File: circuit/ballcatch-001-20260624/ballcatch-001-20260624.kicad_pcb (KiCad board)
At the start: 2 copper layers, 55.6 x 32.2 mm, 5 parts, among them J1 Conn_01x03_Pin, Q1 Q_Photo_NPN_CE

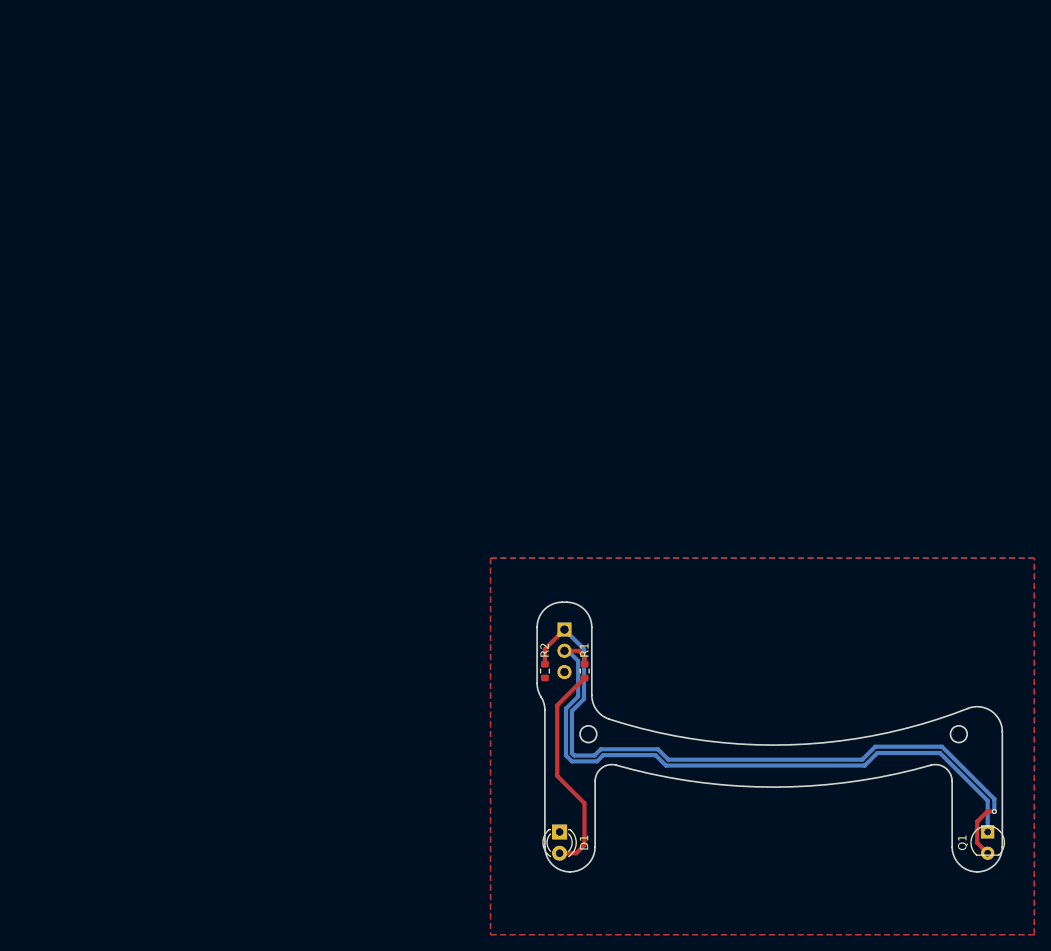
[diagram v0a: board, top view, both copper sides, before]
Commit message: Update ボール補足センサのDR完了、JLCPCBのロゴ追加
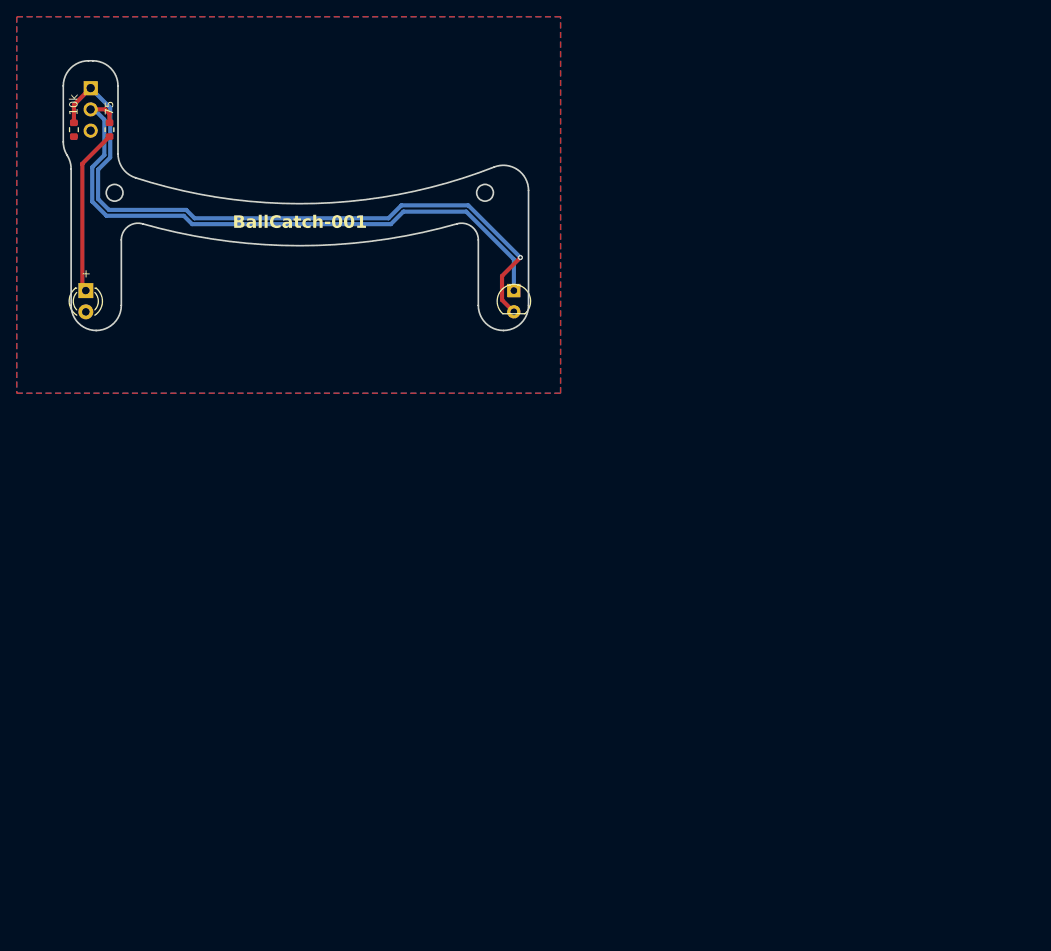
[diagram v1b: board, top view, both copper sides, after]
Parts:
- moved R1 86.1 mm to (26.5, 38.5)
- moved D1 86.0 mm to (23.7, 57.7)
- moved J1 86.0 mm to (24.2, 33.5)
- moved Q1 86.0 mm to (74.8, 59.0)
- moved R2 85.8 mm to (22.2, 38.5)
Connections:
- net signal renamed BallCatch_{Back}
- D1 pad 1: GND -> Net-(D1-A)
- D1 pad 2: Net-(D1-A) -> GND
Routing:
- net Net-(D1-A): track 26.0 -> 19.9 mm
- net BallCatch_{Back}: track 84.5 -> 82.4 mm
- net +3.3V: track 75.9 -> 74.3 mm
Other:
- board text added: "+"
- board text added: "BallCatch-001"
